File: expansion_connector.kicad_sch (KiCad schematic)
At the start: 36 parts, among them J18 ASP-218650-01_mounting_holes, J8 Plug_Samtec_UMPT_1x6_UMPT-06-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, U2 AT24CS01_SOIC8

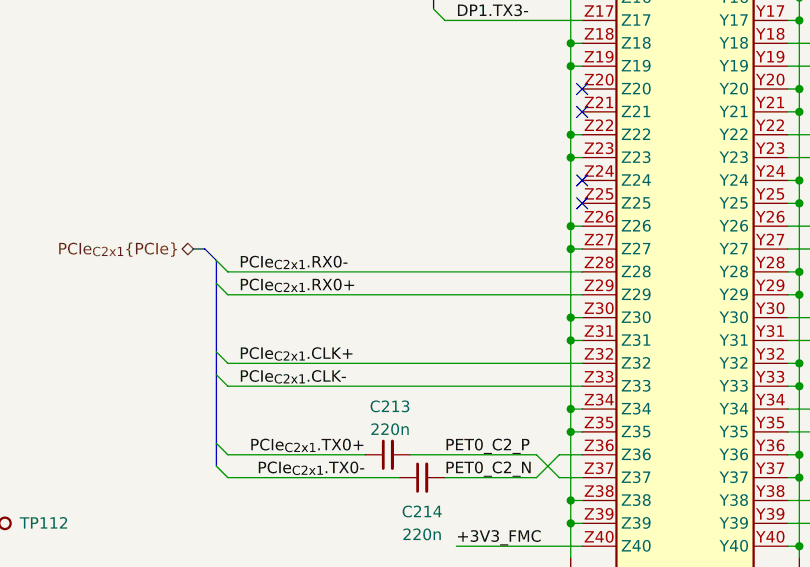
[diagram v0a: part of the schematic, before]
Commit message: [#85702] Added 0R to PCIe x1 on FMC+
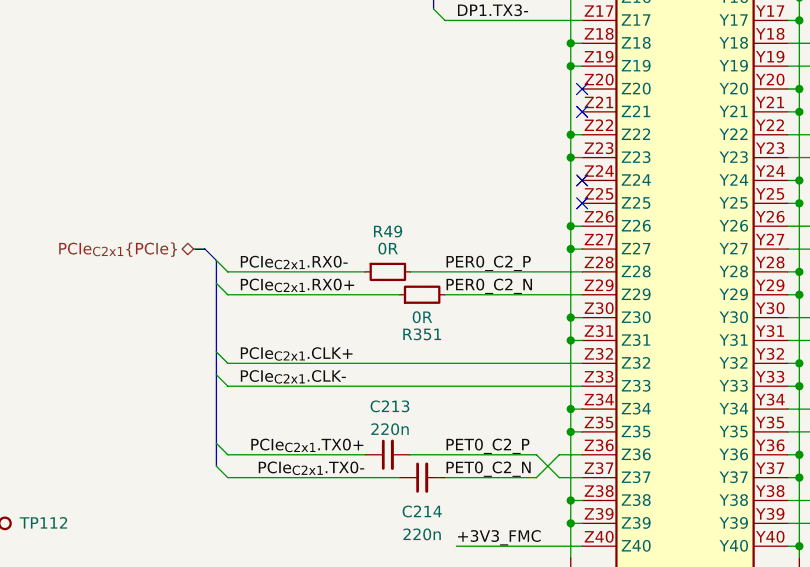
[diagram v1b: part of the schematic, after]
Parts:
- added R351, R49: R_0R_0402, antmicro-footprints:R_0402_1005Metric, symbol antmicroResistors0402:R_0R_0402
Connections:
- net PCIe_{C2x1}.RX0+: now also R351.1; no longer J18.Z29
- net PCIe_{C2x1}.RX0-: now also R49.1; no longer J18.Z28
- new net PER0_C2_N: J18.Z29, R351.2
- new net PER0_C2_P: J18.Z28, R49.2

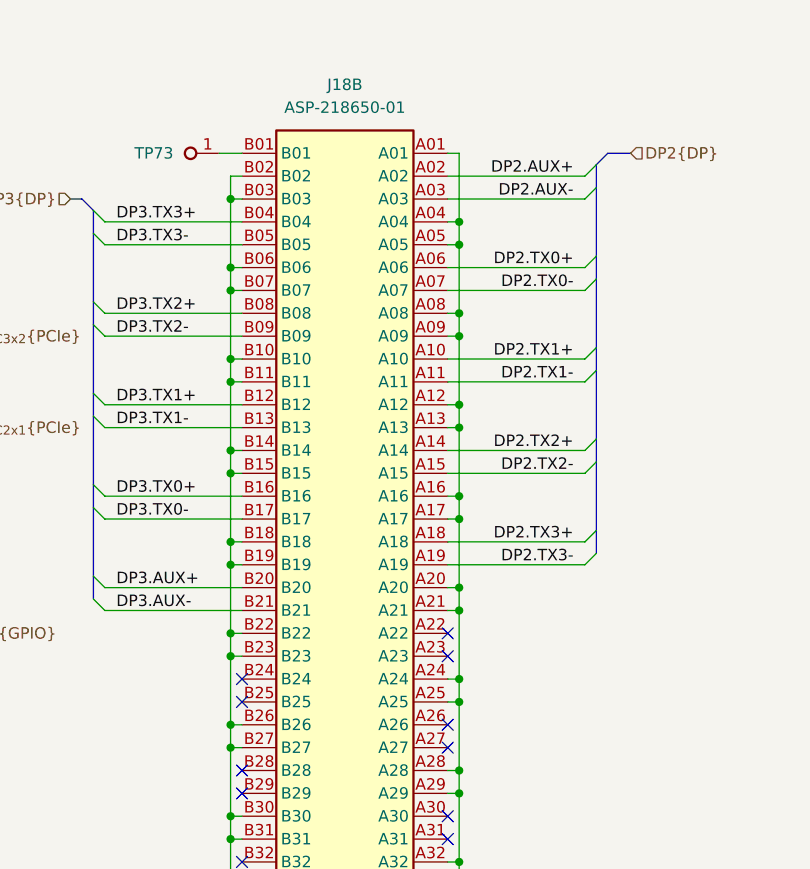
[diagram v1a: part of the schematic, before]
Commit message: [#85702] Start implementing FMC routing changes
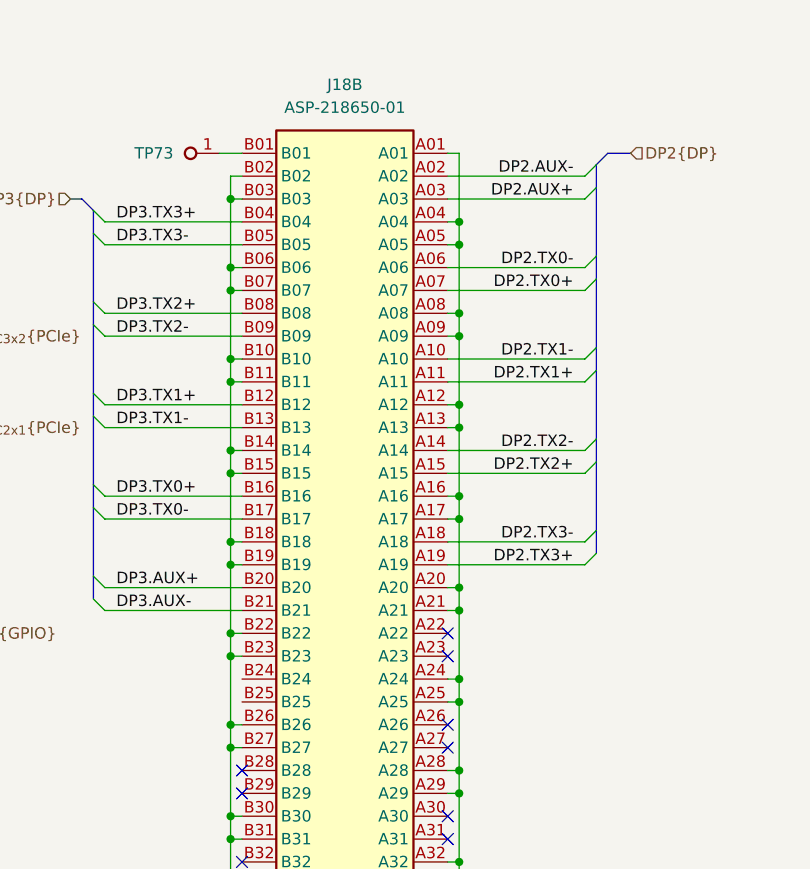
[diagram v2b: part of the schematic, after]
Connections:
- net DP2.AUX+: now also J18.A03; no longer J18.A02
- net DP2.AUX-: now also J18.A02; no longer J18.A03
- net DP2.TX0+: now also J18.A07; no longer J18.A06
- net DP2.TX0-: now also J18.A06; no longer J18.A07
- net DP2.TX1+: now also J18.A11; no longer J18.A10
- net DP2.TX1-: now also J18.A10; no longer J18.A11
- net DP2.TX2+: now also J18.A15; no longer J18.A14
- net DP2.TX2-: now also J18.A14; no longer J18.A15
- net DP2.TX3+: now also J18.A19; no longer J18.A18
- net DP2.TX3-: now also J18.A18; no longer J18.A19
- no-connect marks 181 -> 179
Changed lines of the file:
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@@
 	)
 	(no_connect
-		(at 330.2 87.63)
-	)
-	(no_connect
 		(at 86.36 39.37)
 	)
@@
 	)
 	(no_connect
-		(at 330.2 90.17)
-	)
-	(no_connect
 		(at 109.22 118.11)
 	)
@@
 	)
 	(label "DP2.AUX-"
-		(at 367.03 34.29 180)
+		(at 367.03 31.75 180)
 		(effects
 			(font
@@
 	)
 	(label "DP2.TX3-"
-		(at 367.03 74.93 180)
+		(at 367.03 72.39 180)
 		(effects
 			(font
@@
 	)
 	(label "DP2.TX1+"
-		(at 367.03 52.07 180)
+		(at 367.03 54.61 180)
 		(effects
 			(font
@@
 	)
 	(label "DP2.TX3+"
-		(at 367.03 72.39 180)
+		(at 367.03 74.93 180)
 		(effects
 			(font
@@
 	)
 	(label "DP2.TX2+"
-		(at 367.03 62.23 180)
+		(at 367.03 64.77 180)
 		(effects
 			(font
@@
 	)
 	(label "DP2.AUX+"
-		(at 367.03 31.75 180)
+		(at 367.03 34.29 180)
 		(effects
 			(font
@@
 	)
 	(label "DP2.TX1-"
-		(at 367.03 54.61 180)
+		(at 367.03 52.07 180)
 		(effects
 			(font
@@
 	)
 	(label "DP2.TX0+"
-		(at 367.03 41.91 180)
+		(at 367.03 44.45 180)
 		(effects
 			(font
@@
 	)
 	(label "DP2.TX0-"
-		(at 367.03 44.45 180)
+		(at 367.03 41.91 180)
 		(effects
 			(font
@@
 	)
 	(label "DP2.TX2-"
-		(at 367.03 64.77 180)
+		(at 367.03 62.23 180)
 		(effects
 			(font

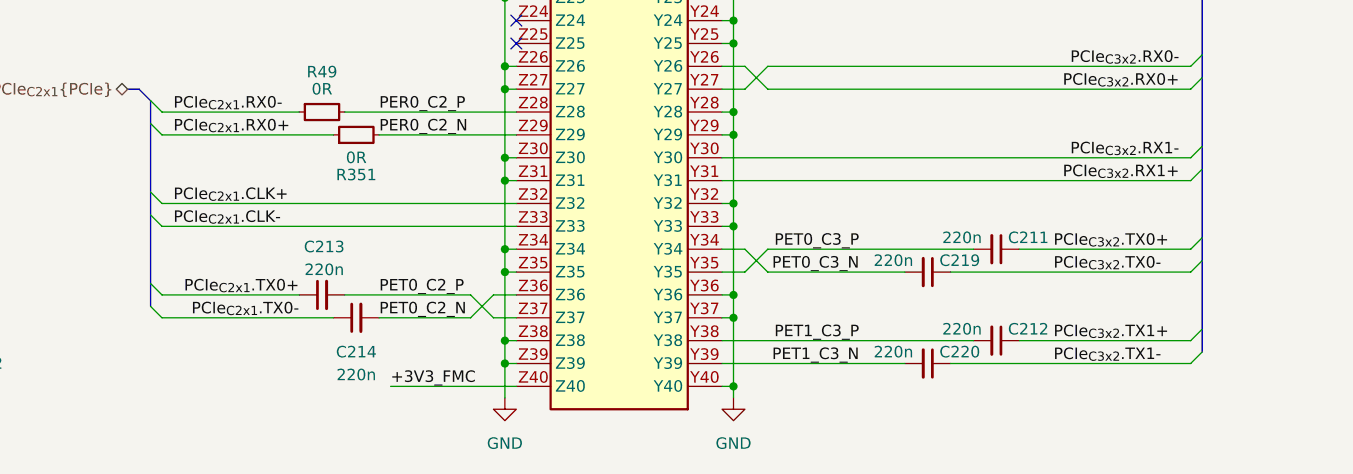
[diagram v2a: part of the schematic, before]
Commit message: [#85702] Start low speed rotuing of FMC+ changes
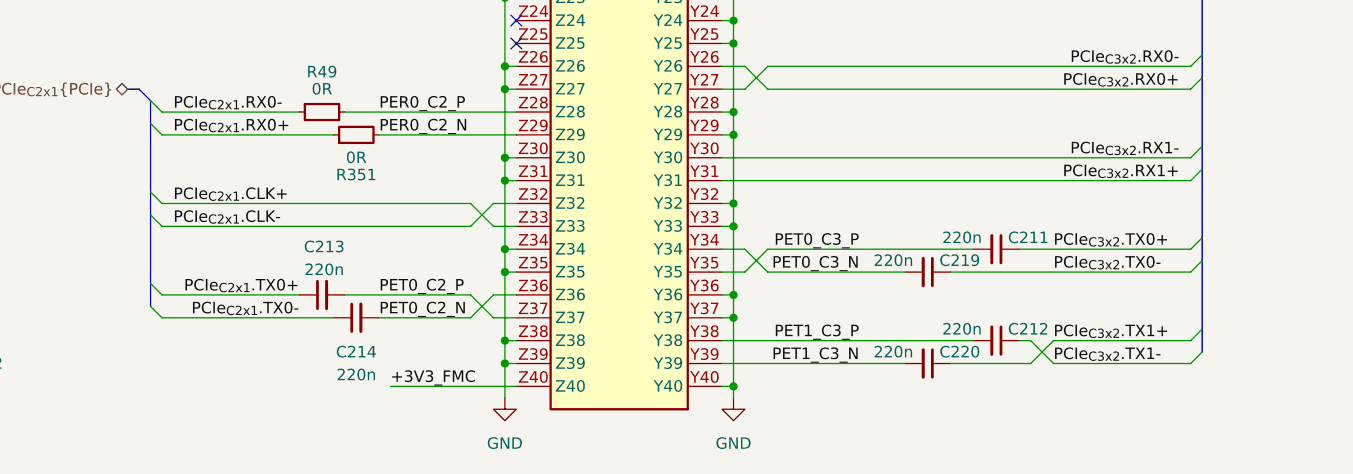
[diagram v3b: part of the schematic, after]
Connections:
- net PCIe_{C2x1}.CLK+: now also J18.Z33; no longer J18.Z32
- net PCIe_{C2x1}.CLK-: now also J18.Z32; no longer J18.Z33
- net PCIe_{C3x2}.TX1+: now also C220.1; no longer C212.1
- net PCIe_{C3x2}.TX1-: now also C212.1; no longer C220.1
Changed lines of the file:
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@@
 	(wire
 		(pts
+			(xy 270.51 250.19) (xy 261.62 250.19)
+		)
+		(stroke
+			(width 0)
+			(type default)
+		)
+	)
+	(wire
+		(pts
 			(xy 110.49 85.09) (xy 110.49 92.71)
 		)
@@
 	(wire
 		(pts
+			(xy 208.28 234.95) (xy 210.82 232.41)
+		)
+		(stroke
+			(width 0)
+			(type default)
+		)
+	)
+	(wire
+		(pts
 			(xy 166.37 95.25) (xy 166.37 102.87)
 		)
@@
 	(wire
 		(pts
-			(xy 288.29 250.19) (xy 261.62 250.19)
+			(xy 288.29 250.19) (xy 273.05 250.19)
 		)
 		(stroke
@@
 	(wire
 		(pts
-			(xy 288.29 247.65) (xy 269.24 247.65)
+			(xy 288.29 247.65) (xy 273.05 247.65)
 		)
 		(stroke
@@
 	(wire
 		(pts
-			(xy 173.99 232.41) (xy 213.36 232.41)
+			(xy 173.99 232.41) (xy 208.28 232.41)
 		)
 		(stroke
@@
 		)
 	)
+	(wire
+		(pts
+			(xy 210.82 234.95) (xy 213.36 234.95)
+		)
+		(stroke
+			(width 0)
+			(type default)
+		)
+	)
 	(bus
 		(pts
@@
 	(wire
 		(pts
-			(xy 173.99 234.95) (xy 213.36 234.95)
+			(xy 173.99 234.95) (xy 208.28 234.95)
 		)
 		(stroke
@@
 		)
 	)
+	(wire
+		(pts
+			(xy 270.51 250.19) (xy 273.05 247.65)
+		)
+		(stroke
+			(width 0)
+			(type default)
+		)
+	)
 	(bus
 		(pts
@@
 	(wire
 		(pts
+			(xy 270.51 247.65) (xy 269.24 247.65)
+		)
+		(stroke
+			(width 0)
+			(type default)
+		)
+	)
+	(wire
+		(pts
 			(xy 97.79 242.57) (xy 97.79 243.84)
 		)
@@
 	(wire
 		(pts
+			(xy 208.28 232.41) (xy 210.82 234.95)
+		)
+		(stroke
+			(width 0)
+			(type default)
+		)
+	)
+	(wire
+		(pts
 			(xy 353.06 87.63) (xy 354.33 87.63)
 		)
@@
 	(wire
 		(pts
+			(xy 270.51 247.65) (xy 273.05 250.19)
+		)
+		(stroke
+			(width 0)
+			(type default)
+		)
+	)
+	(wire
+		(pts
 			(xy 57.15 222.25) (xy 57.15 224.79)
 		)
@@
 		)
 		(stroke
+			(width 0)
+			(type default)
+		)
+	)
+	(wire
+		(pts
+			(xy 210.82 232.41) (xy 213.36 232.41)
+		)
+		(stroke

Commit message: [#85702] Finish FMC+ layout changes
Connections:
- net PCIe_{C3x2}.CLK+: now also J18.Y23; no longer J18.Y22
- net PCIe_{C3x2}.CLK-: now also J18.Y22; no longer J18.Y23
- net PCIe_{C3x2}.RX1+: now also J18.Y30; no longer J18.Y31
- net PCIe_{C3x2}.RX1-: now also J18.Y31; no longer J18.Y30
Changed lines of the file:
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@@
 		)
 	)
+	(wire
+		(pts
+			(xy 236.22 209.55) (xy 288.29 209.55)
+		)
+		(stroke
+			(width 0)
+			(type default)
+		)
+	)
 	(bus
 		(pts
@@
 	(wire
 		(pts
-			(xy 288.29 207.01) (xy 241.3 207.01)
-		)
-		(stroke
-			(width 0)
-			(type default)
-		)
-	)
-	(wire
-		(pts
 			(xy 248.92 115.57) (xy 236.22 115.57)
 		)
@@
 	(wire
 		(pts
+			(xy 236.22 207.01) (xy 288.29 207.01)
+		)
+		(stroke
+			(width 0)
+			(type default)
+		)
+	)
+	(wire
+		(pts
 			(xy 58.42 163.83) (xy 57.15 163.83)
 		)
@@
 	(wire
 		(pts
+			(xy 241.3 229.87) (xy 238.76 227.33)
+		)
+		(stroke
+			(width 0)
+			(type default)
+		)
+	)
+	(wire
+		(pts
 			(xy 119.38 173.99) (xy 120.65 173.99)
 		)
@@
 	(wire
 		(pts
-			(xy 241.3 207.01) (xy 238.76 209.55)
-		)
-		(stroke
-			(width 0)
-			(type default)
-		)
-	)
-	(wire
-		(pts
 			(xy 127 80.01) (xy 109.22 80.01)
 		)
@@
 	(wire
 		(pts
-			(xy 288.29 209.55) (xy 241.3 209.55)
-		)
-		(stroke
-			(width 0)
-			(type default)
-		)
-	)
-	(wire
-		(pts
 			(xy 247.65 67.31) (xy 247.65 74.93)
 		)
@@
 	(wire
 		(pts
-			(xy 238.76 209.55) (xy 236.22 209.55)
-		)
-		(stroke
-			(width 0)
-			(type default)
-		)
-	)
-	(wire
-		(pts
 			(xy 326.39 176.53) (xy 335.28 176.53)
 		)
@@
 		)
 	)
-	(wire
-		(pts
-			(xy 241.3 209.55) (xy 238.76 207.01)
-		)
-		(stroke
-			(width 0)
-			(type default)
-		)
-	)
 	(bus
 		(pts
@@
 	(wire
 		(pts
-			(xy 238.76 207.01) (xy 236.22 207.01)
-		)
-		(stroke
-			(width 0)
-			(type default)
-		)
-	)
-	(wire
-		(pts
 			(xy 119.38 173.99) (xy 119.38 181.61)
 		)
@@
 	(wire
 		(pts
+			(xy 238.76 229.87) (xy 236.22 229.87)
+		)
+		(stroke
+			(width 0)
+			(type default)
+		)
+	)
+	(wire
+		(pts
 			(xy 353.06 87.63) (xy 354.33 87.63)
 		)
@@
 	(wire
 		(pts
+			(xy 241.3 227.33) (xy 238.76 229.87)
+		)
+		(stroke
+			(width 0)
+			(type default)
+		)
+	)
+	(wire
+		(pts
 			(xy 144.78 179.07) (xy 143.51 179.07)
 		)
@@
 	(wire
 		(pts
-			(xy 288.29 229.87) (xy 236.22 229.87)
+			(xy 288.29 229.87) (xy 241.3 229.87)
 		)
 		(stroke
@@
 	(wire
 		(pts
-			(xy 288.29 227.33) (xy 236.22 227.33)
+			(xy 288.29 227.33) (xy 241.3 227.33)
 		)
 		(stroke
@@
 		)
 		(stroke
+			(width 0)
+			(type default)
+		)
+	)
+	(wire
+		(pts
+			(xy 238.76 227.33) (xy 236.22 227.33)
+		)
+		(stroke

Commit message: Update naming on schematic sheets and PCB, update release date
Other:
- title: Jetson AGX Thor Baseboard -> Antmicro Baseboard for Jetson AGX Thor
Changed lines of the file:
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@@
 	(paper "A3")
 	(title_block
-		(title "Jetson AGX Thor Baseboard")
-		(date "2025-11-03")
+		(title "Antmicro Baseboard for Jetson AGX Thor")
+		(date "2026-02-17")
 		(rev "1.1.0")
 		(company "Antmicro Ltd")

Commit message: [#88665] SFP connector footprint position fix, UMPT-06-06.5-G-V-S-W-TR symbol updated from library
1. SFP connector position fix due to footprint modification in library
2. Component UMPT-06-06.5-G-V-S-W-TR updated from library after fix
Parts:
- J8: footprint antmicro-footprints:Conn_Plug_Samtec_UMPT_1x6_UMPT-06-06.5-G-V-S-TR -> antmicro-footprints:Conn_Plug_Samtec_UMPT_1x6_UMPT-06-06.5-G-V-S-W-TR; symbol antmicroB2BConnectors:Plug_Samtec_UMPT_1x6_UMPT-06-06.5-G-V-S-TR -> antmicroB2BConnectors:Plug_Samtec_UMPT_1x6_UMPT-06-06.5-G-V-S-W-TR
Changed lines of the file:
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@@
 	)
 	(symbol
-		(lib_id "antmicroB2BConnectors:Plug_Samtec_UMPT_1x6_UMPT-06-06.5-G-V-S-TR")
+		(lib_id "antmicroB2BConnectors:Plug_Samtec_UMPT_1x6_UMPT-06-06.5-G-V-S-W-TR")
 		(at 337.82 223.52 0)
 		(mirror y)
@@
 			)
 		)
-		(property "Footprint" "antmicro-footprints:Conn_Plug_Samtec_UMPT_1x6_UMPT-06-06.5-G-V-S-TR"
+		(property "Footprint" "antmicro-footprints:Conn_Plug_Samtec_UMPT_1x6_UMPT-06-06.5-G-V-S-W-TR"
 			(at 314.96 233.68 0)
 			(effects
